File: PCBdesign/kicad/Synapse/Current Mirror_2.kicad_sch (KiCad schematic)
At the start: 5 parts, among them IC3 ALD1105PBL

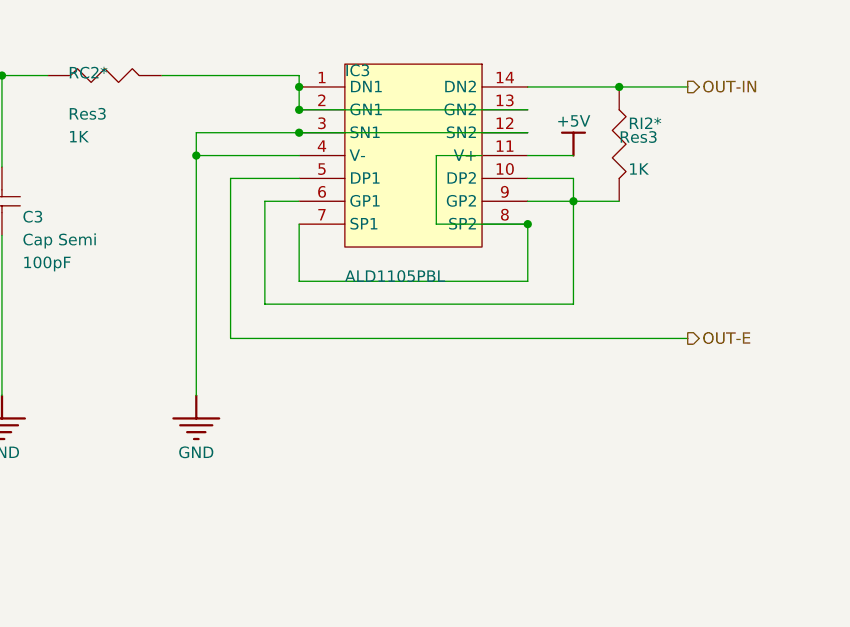
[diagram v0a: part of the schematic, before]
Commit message: update schematics for replacing ALD w/ discrete BJTs
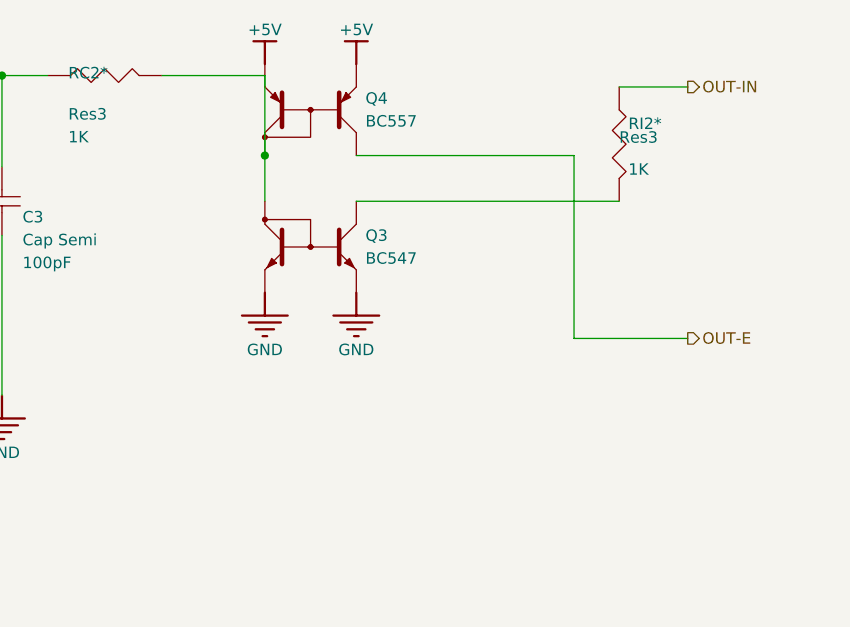
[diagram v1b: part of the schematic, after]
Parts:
- removed IC3: ALD1105PBL, C__Users_86135_Documents_AltiumLL_SamacSys.PcbLib:DIP762W51P254L1828H508Q14N, symbol *:2_0_ALD1105PBL_*
- added Q3: BC547, symbol Device:Q_NPN_CurrentMirror
- added Q4: BC557, symbol Device:Q_PNP_CurrentMirror
- C3: LATESTREVISIONDATE 29-May-2009 -> (none); LATESTREVISIONNOTE IPC-7351 Footprint Added. -> (none); PACKAGEDESCRIPTION Chip Capacitor -> (none); PACKAGEREFERENCE C1206 -> (none); PUBLISHED 8-Jun-2000 -> (none); PUBLISHER Altium Limited -> (none)
- C4: PACKAGEDESCRIPTION Capacitor; 2 Leads -> (none); PACKAGEREFERENCE CAPR5-4X5 -> (none); PUBLISHED 23-Sep-2002 -> (none); PUBLISHER Altium Limited -> (none)
- RC2*, RI2*: LATESTREVISIONDATE 29-May-2009 -> (none); LATESTREVISIONNOTE IPC-7351 Footprint Added. -> (none); PACKAGEDESCRIPTION Chip Resistor -> (none); PACKAGEREFERENCE J1-0603 -> (none); PUBLISHED 8-Jun-2000 -> (none); PUBLISHER Altium Limited -> (none)
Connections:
- net +5V: now also Q4.E1, Q4.E2
- net GND: now also Q3.E1, Q3.E2
- net OUT-E: now also Q4.C1
- net at RI2*.2: now also Q3.C1
- net at RC2*.2: now also Q3.C2, Q4.C2

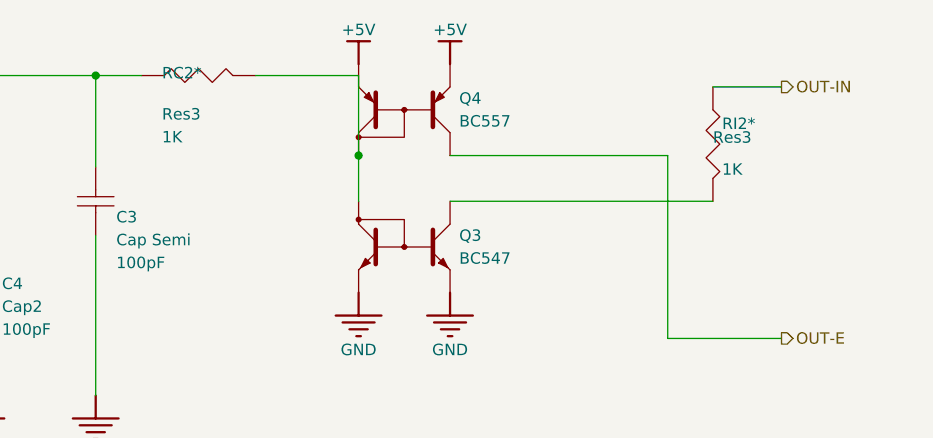
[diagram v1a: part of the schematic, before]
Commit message: Add annotation script, wiring checklist for breadboarding, and .gitignore in case proprietary libs are added. Fix annotations that were missing after KiCad import in the schematics.
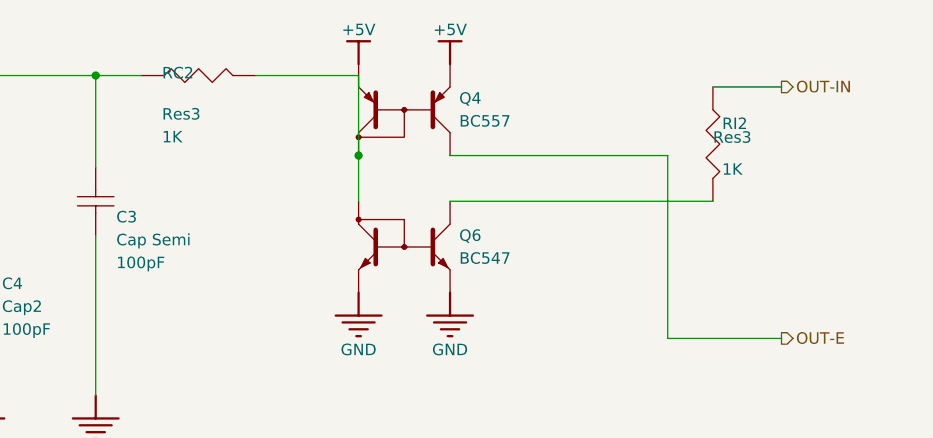
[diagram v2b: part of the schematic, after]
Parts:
- renumbered Q3 to Q6, RC2* to RC2, RI2* to RI2
